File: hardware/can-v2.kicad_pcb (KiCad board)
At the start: 2 copper layers, 45 x 35 mm, 42 parts, among them K1 CONN_3, P1 CON-SENSOR, P2 Debug, P3 Boot, SW1 Termination, U1 XMC1404, U2 MCP2562, U3 DRILL, U4 DRILL, U5 DRILL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

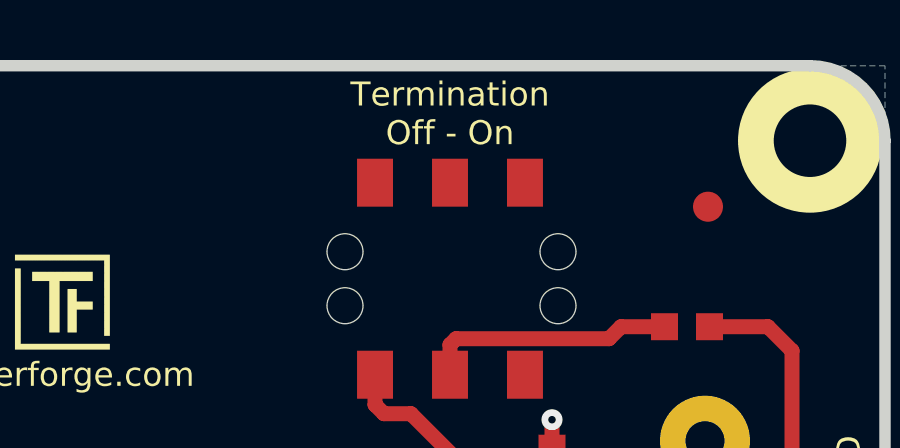
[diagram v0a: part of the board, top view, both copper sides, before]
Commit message: fix termination text
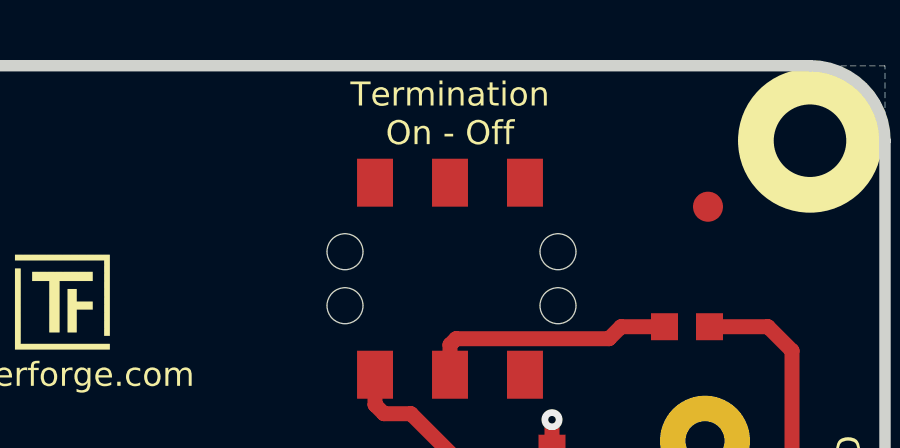
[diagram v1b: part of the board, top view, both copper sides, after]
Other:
- board text added: "Termination On - Off"
- board text removed: "Termination Off - On"
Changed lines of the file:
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@@
-(kicad_pcb (version 4) (host pcbnew 4.0.2+dfsg1-stable)
+(kicad_pcb (version 4) (host pcbnew 4.0.7-e2-6376~61~ubuntu18.04.1)
   (general
     (links 77)
     (no_connects 0)
-    (area 125.109499 82.909499 170.490501 118.290501)
+    (area 124.445139 82.245139 282.795857 162.890793)
     (thickness 1.6002)
     (drawings 16)
@@
     (effects (font (size 0.8001 0.8001) (thickness 0.14986)))
   )
-  (gr_text "Termination\nOff - On" (at 155.8 84.7) (layer F.SilkS)
+  (gr_text "Termination\nOn - Off" (at 155.8 84.7) (layer F.SilkS)
     (effects (font (size 0.8 0.8) (thickness 0.15)))
   )

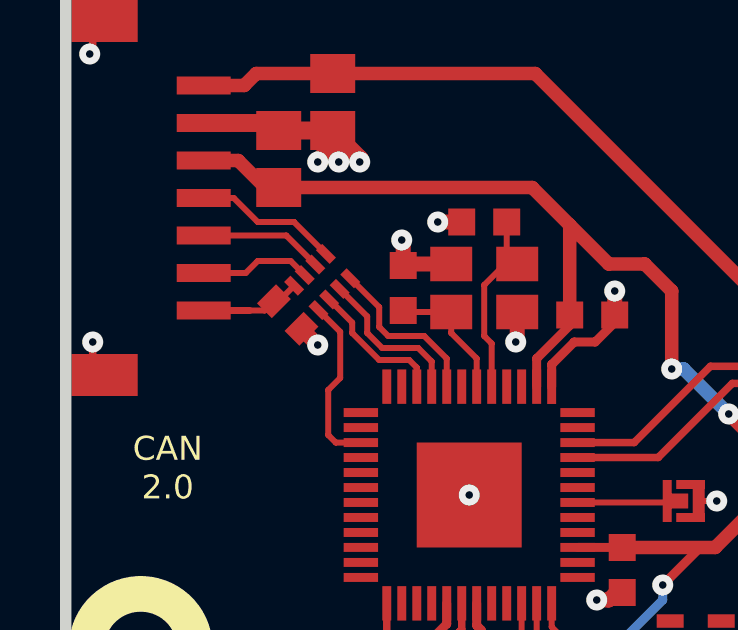
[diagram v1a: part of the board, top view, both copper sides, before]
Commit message: Change capacitor footprint(s) to C0402F
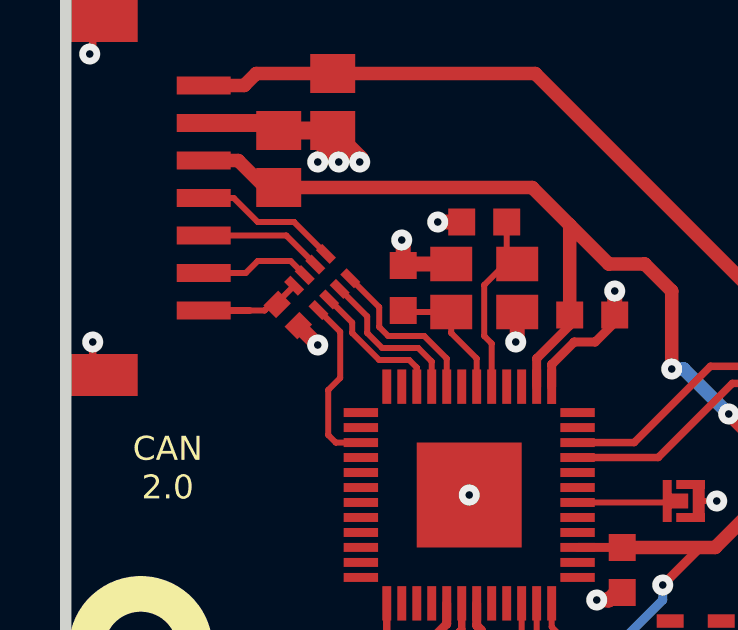
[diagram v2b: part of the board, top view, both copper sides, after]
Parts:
- C1: footprint C0402E -> kicad-libraries:C0402F
- D1, D2, D3: footprint D0603F -> kicad-libraries:D0603F
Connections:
- RP2 pad 1: (no net) -> Net-(RP2-Pad1)
- RP2 pad 8: (no net) -> Net-(RP2-Pad8)
- U1 pad 1: (no net) -> Net-(U1-Pad1)
- U1 pad 10: (no net) -> Net-(U1-Pad10)
- U1 pad 11: (no net) -> Net-(U1-Pad11)
- U1 pad 12: (no net) -> Net-(U1-Pad12)
- U1 pad 14: (no net) -> Net-(U1-Pad14)
- U1 pad 15: (no net) -> Net-(U1-Pad15)
- U1 pad 16: (no net) -> Net-(U1-Pad16)
- U1 pad 2: (no net) -> Net-(U1-Pad2)
- U1 pad 20: (no net) -> Net-(U1-Pad20)
- U1 pad 21: (no net) -> Net-(U1-Pad21)
- U1 pad 25: (no net) -> Net-(U1-Pad25)
- U1 pad 26: (no net) -> Net-(U1-Pad26)
- U1 pad 28: (no net) -> Net-(U1-Pad28)
- U1 pad 29: (no net) -> Net-(U1-Pad29)
- U1 pad 31: (no net) -> Net-(U1-Pad31)
- U1 pad 32: (no net) -> Net-(U1-Pad32)
- U1 pad 35: (no net) -> Net-(U1-Pad35)
- U1 pad 36: (no net) -> Net-(U1-Pad36)
- U1 pad 39: (no net) -> Net-(U1-Pad39)
- U1 pad 4: (no net) -> Net-(U1-Pad4)
- U1 pad 40: (no net) -> Net-(U1-Pad40)
- U1 pad 43: (no net) -> Net-(U1-Pad43)
- U1 pad 47: (no net) -> Net-(U1-Pad47)
- U1 pad 48: (no net) -> Net-(U1-Pad48)
- U1 pad 5: (no net) -> Net-(U1-Pad5)
- U1 pad 6: (no net) -> Net-(U1-Pad6)
- U1 pad 7: (no net) -> Net-(U1-Pad7)
- U1 pad 8: (no net) -> Net-(U1-Pad8)
- U1 pad 9: (no net) -> Net-(U1-Pad9)
